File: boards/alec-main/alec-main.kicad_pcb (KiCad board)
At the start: 4 copper layers, 64 x 56 mm, 125 parts, among them J1 Conn_01x02_Pin, J2 USB_C_Receptacle_USB2.0_16P, J3 Conn_01x02_Pin, J4 Conn_01x04_Pin, J5 BM07B-GHS-TBT, J6 BM06B-GHS-TBT, J7 UNPOPULATED_TEST_PADS, Q1 AO3401A, Q2 AO3401A, Q3 MMBT3904, Q4 MMBT3904, Q5 MMBT3904, Q6 AO3401A, Q7 MMBT3904, SW2 RESET, SW3 BOOT, U1 TPS63070RNMR, U2 TPS63070RNMR, U3 ESP32-S3-WROOM-1-N16, U4 USBLC6-2SC6, U5 RV-3028-C7, U6 MAX98357A, U7 SN74LVC2G66DCUR, U8 SN74LVC1T45DBVR

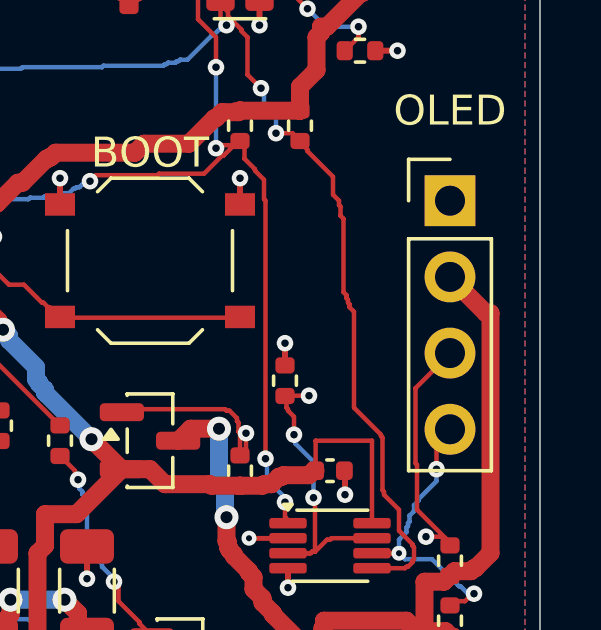
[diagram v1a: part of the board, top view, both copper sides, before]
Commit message: fix(rooster): allow finished-hole tolerance at main display header
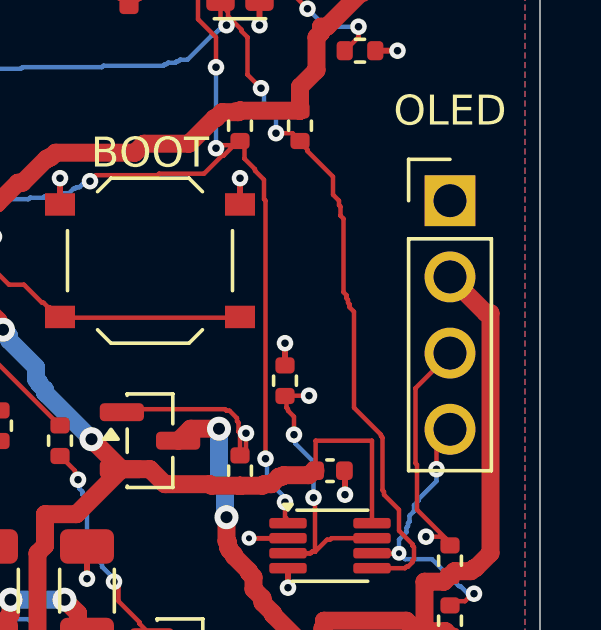
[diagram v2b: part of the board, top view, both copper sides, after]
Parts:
- J4: footprint Connector_PinHeader_2.54mm:PinHeader_1x04_P2.54mm_Vertical -> Board:Samtec_TSW-104-07-G-S_Drill1.10mm
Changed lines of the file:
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@@
 		(property "LCSC#" "C84416" (at 0 0 0) (layer "F.Fab") (hide yes) (effects (font (size 1 1) (thickness 0.15))))
 	)
-	(footprint "Connector_PinHeader_2.54mm:PinHeader_1x04_P2.54mm_Vertical"
+	(footprint "Board:Samtec_TSW-104-07-G-S_Drill1.10mm"
 		(layer "F.Cu")
 		(at 161 86)
-		(descr "Through hole straight pin header, 1x04, 2.54mm pitch, single row")
+		(descr "Samtec TSW-104-07-G-S, four 1.10mm finished holes for JLCPCB tolerance; 1.70mm lands, 2.54mm pitch")
 		(tags "Through hole pin header THT 1x04 2.54mm single row")
 		(property "Reference" "J4"
@@
 			(at 0 0)
 			(size 1.7 1.7)
-			(drill 1)
+			(drill 1.1)
 			(layers "*.Cu" "*.Mask")
 			(remove_unused_layers no)
@@
 			(at 0 2.54)
 			(size 1.7 1.7)
-			(drill 1)
+			(drill 1.1)
 			(layers "*.Cu" "*.Mask")
 			(remove_unused_layers no)
@@
 			(at 0 5.08)
 			(size 1.7 1.7)
-			(drill 1)
+			(drill 1.1)
 			(layers "*.Cu" "*.Mask")
 			(remove_unused_layers no)
@@
 			(at 0 7.62)
 			(size 1.7 1.7)
-			(drill 1)
-			(layers "*.Cu" "*.Mask")
-			(remove_unused_layers no)
+			(drill 1.1)
+			(layers "*.Cu" "*.Mask")
+			(remove_unused_layers no)
